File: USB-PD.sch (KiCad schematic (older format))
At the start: 59 parts, among them IC3 TPS7A0518PDBVT, J1 1053131102, J11 E8124-015-01, Q10 Si7223DN, Q11 Si7223DN, Q12 BSS84AKW, Q14 BSS84AKW, Q9 SQS401EN-T1_BE3, U12 STUSB4500QTR, U14 LTC4418IUF#PBF

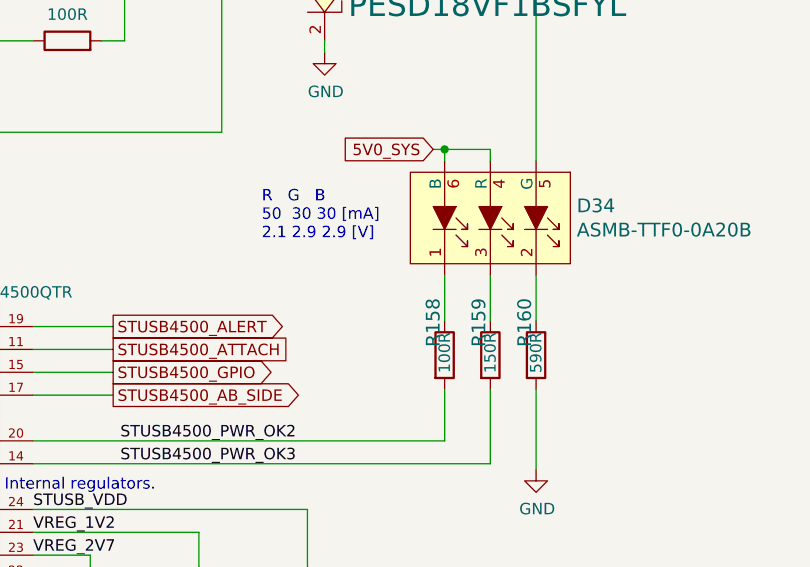
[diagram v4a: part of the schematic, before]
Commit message: Corrected errors from feedback. Added board name, version, Antmicro and OSHW logo, connector labels, button and LED descriptions
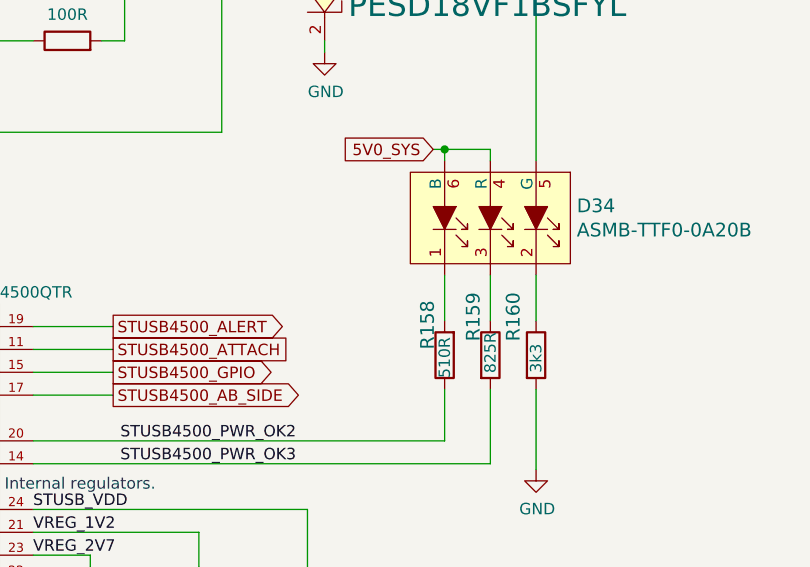
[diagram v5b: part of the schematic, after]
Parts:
- removed R158: R_100R_0402, sc606-baseboard-footprints:0402-res, symbol sc606-baseboard:R_100R_0402
- removed R159: R_150R_0402, sc606-baseboard-footprints:0402-res, symbol sc606-baseboard:R_150R_0402
- removed R160: R_590R_0402, sc606-baseboard-footprints:0402-res, symbol sc606-baseboard:R_590R_0402
- added R158: R_510R_0402, antmicro-footprints:0402-res, symbol antmicroResistors0402:R_510R_0402
- added R159: R_825R_0402, antmicro-footprints:0402-res, symbol antmicroResistors0402:R_825R_0402
- added R160: R_3k3_0402, antmicro-footprints:0402-res, symbol antmicroResistors0402:R_3k3_0402
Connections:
- net GND: now also R160.2
- net STUSB4500_PWR_OK2: now also R158.1
- net STUSB4500_PWR_OK3: now also R159.2
- net at D34.1: now also R158.2
- net at D34.2: now also R160.1
- net at D34.3: now also R159.1
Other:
- note removed: "R G B\n50 30 30 [mA]\n2.1 2.9 2.9 [V]"
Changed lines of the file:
@@
-	0    1    1    0
-$EndComp
-$Comp
-L sc606-baseboard:R_100R_0402 R158
-U 1 1 6219BF48
-P 9900 2975
-F 0 "R158" H 9650 2925 60  0000 L CNN
-F 1 "R_100R_0402" H 9900 2825 60  0001 C CNN
-F 2 "sc606-baseboard-footprints:0402-res" H 10100 3175 60  0001 L CNN
-F 3 "" H 9900 2975 50  0001 C CNN
-F 4 "BOURNS" H 10100 3375 60  0001 L CNN "Manufacturer"
-F 5 "CR0402-FX-1000GLF" H 10100 3275 60  0001 L CNN "MPN"
-F 6 "100R" H 9800 2975 50  0000 L CNN "Val"
-	1    9900 2975
-	0    1    1    0
-$EndComp
-$Comp
-L sc606-baseboard:R_150R_0402 R159
-U 1 1 62198F27
-P 10100 2975
-F 0 "R159" H 9850 2925 60  0000 L CNN
-F 1 "R_150R_0402" H 10100 2825 60  0001 C CNN
-F 2 "sc606-baseboard-footprints:0402-res" H 10300 3175 60  0001 L CNN
-F 3 "" H 10100 2975 50  0001 C CNN
-F 4 "VISHAY" H 10300 3375 60  0001 L CNN "Manufacturer"
-F 5 "CRCW0402150RFKED" H 10300 3275 60  0001 L CNN "MPN"
-F 6 "150R" H 10000 2975 50  0000 L CNN "Val"
-	1    10100 2975
 	0    1    1    0
 $EndComp
@@
 Wire Wire Line
 	10300 2825 10300 2625
-$Comp
-L sc606-baseboard:R_590R_0402 R160
-U 1 1 621057A9
-P 10300 2975
-F 0 "R160" H 10050 2925 60  0000 L CNN
-F 1 "R_590R_0402" H 10300 2825 60  0001 C CNN
-F 2 "sc606-baseboard-footprints:0402-res" H 10500 3175 60  0001 L CNN
-F 3 "" H 10300 2975 50  0001 C CNN
-F 4 "PANASONIC_ELECTRONIC_COMPONENTS" H 10500 3375 60  0001 L CNN "Manufacturer"
-F 5 "ERJ2RKF5900X" H 10500 3275 60  0001 L CNN "MPN"
-F 6 "590R" H 10200 2975 50  0000 L CNN "Val"
-	1    10300 2975
-	0    1    1    0
-$EndComp
 Text GLabel 9850 2075 0    50   Input ~ 0
 5V0_SYS
-Text Notes 9100 2475 0    50   ~ 0
-R   G   B\n50  30 30 [mA]\n2.1 2.9 2.9 [V]
 Wire Wire Line
 	7650 2000 8925 2000
@@
 	1    0    0    1
 $EndComp
+$Comp
+L antmicroResistors0402:R_510R_0402 R158
+U 1 1 622D2DA1
+P 9900 2975
+F 0 "R158" H 9925 3050 60  0000 L CNN
+F 1 "R_510R_0402" H 9900 2825 60  0001 C CNN
+F 2 "antmicro-footprints:0402-res" H 10100 3175 60  0001 L CNN
+F 3 "" H 9900 2975 50  0001 C CNN
+F 4 "Yageo" H 10100 3375 60  0001 L CNN "Manufacturer"
+F 5 "RC0402JR-07510RL" H 10100 3275 60  0001 L CNN "MPN"
+F 6 "510R" H 9800 2975 50  0000 L CNN "Val"
+	1    9900 2975
+	0    -1   -1   0
+$EndComp
+$Comp
+L antmicroResistors0402:R_825R_0402 R159
+U 1 1 622D800C
+P 10100 2975
+F 0 "R159" H 9825 2900 60  0000 L CNN
+F 1 "R_825R_0402" H 10100 2825 60  0001 C CNN
+F 2 "antmicro-footprints:0402-res" H 10300 3175 60  0001 L CNN
+F 3 "" H 10100 2975 50  0001 C CNN
+F 4 "PANASONIC" H 10300 3375 60  0001 L CNN "Manufacturer"
+F 5 "ERJ2RKF8250X" H 10300 3275 60  0001 L CNN "MPN"
+F 6 "825R" H 10000 2975 50  0000 L CNN "Val"
+	1    10100 2975
+	0    1    1    0
+$EndComp
+$Comp
+L antmicroResistors0402:R_3k3_0402 R160
+U 1 1 623007ED
+P 10300 2975
+F 0 "R160" H 10025 2875 60  0000 L CNN
+F 1 "R_3k3_0402" H 10300 2825 60  0001 C CNN
+F 2 "antmicro-footprints:0402-res" H 10500 3175 60  0001 L CNN
+F 3 "" H 10300 2975 50  0001 C CNN
+F 4 "MULTICOMP PRO" H 10500 3375 60  0001 L CNN "Manufacturer"
+F 5 "MCWR04X3301FTL" H 10500 3275 60  0001 L CNN "MPN"
+F 6 "3k3" H 10250 2975 50  0000 L CNN "Val"
+	1    10300 2975
+	0    1    1    0
+$EndComp
 $EndSCHEMATC

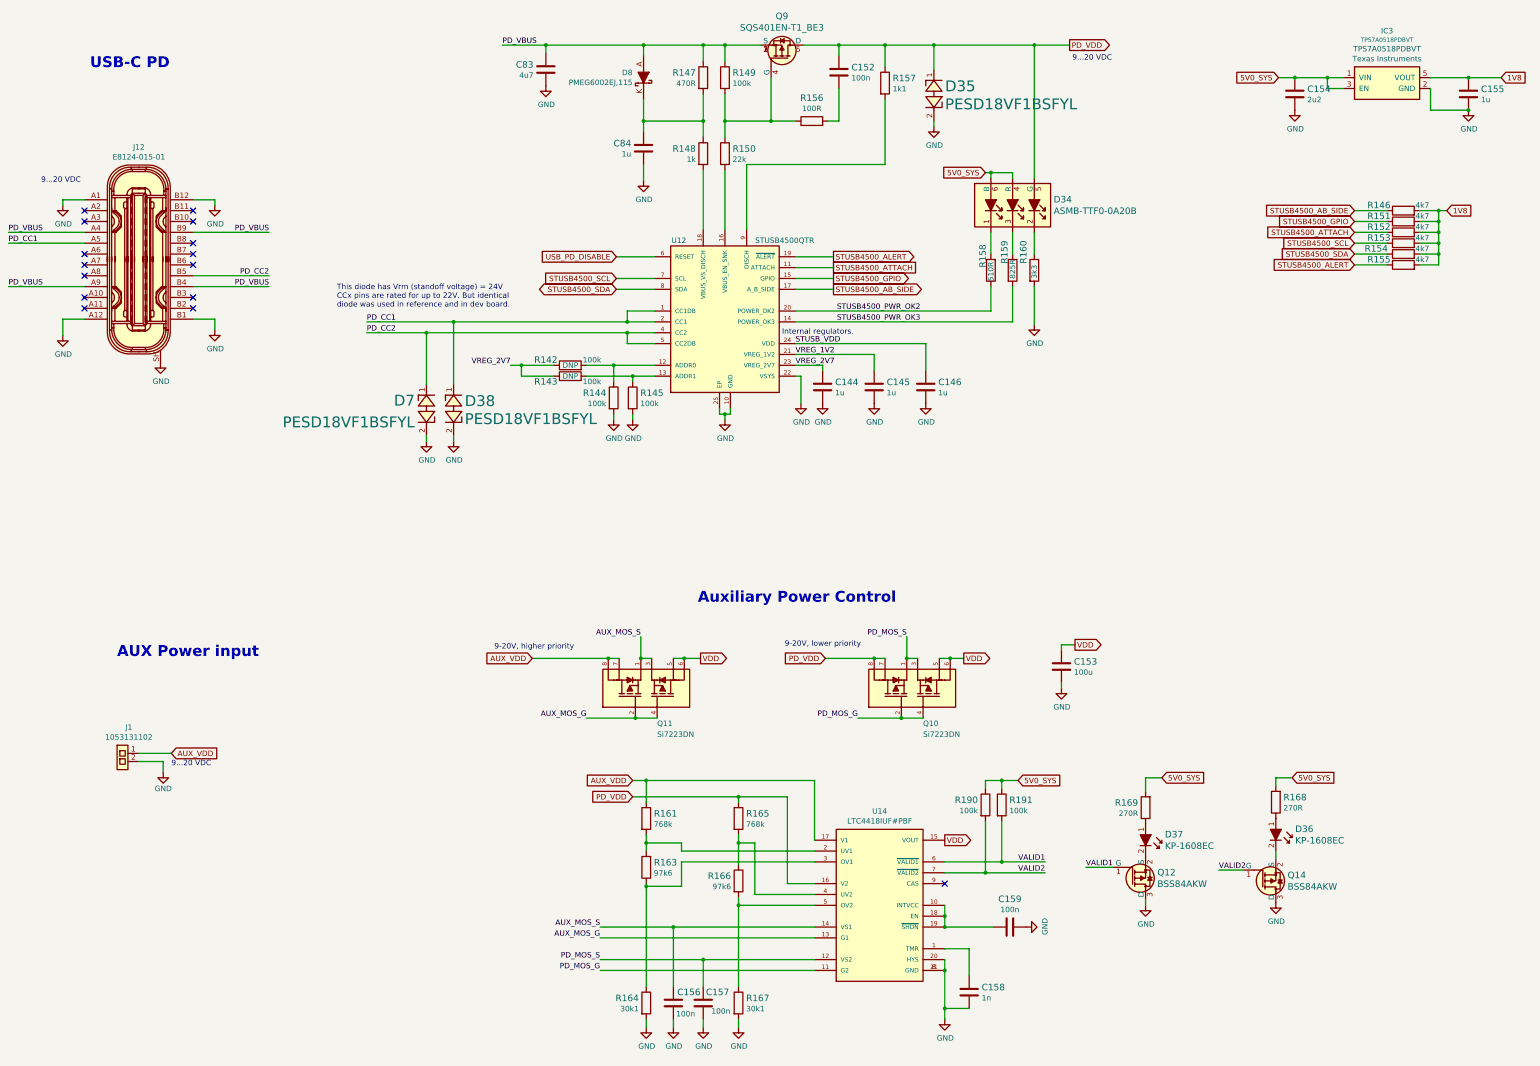
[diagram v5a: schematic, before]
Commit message: Schematic cleanup - peripherals and USB-PD
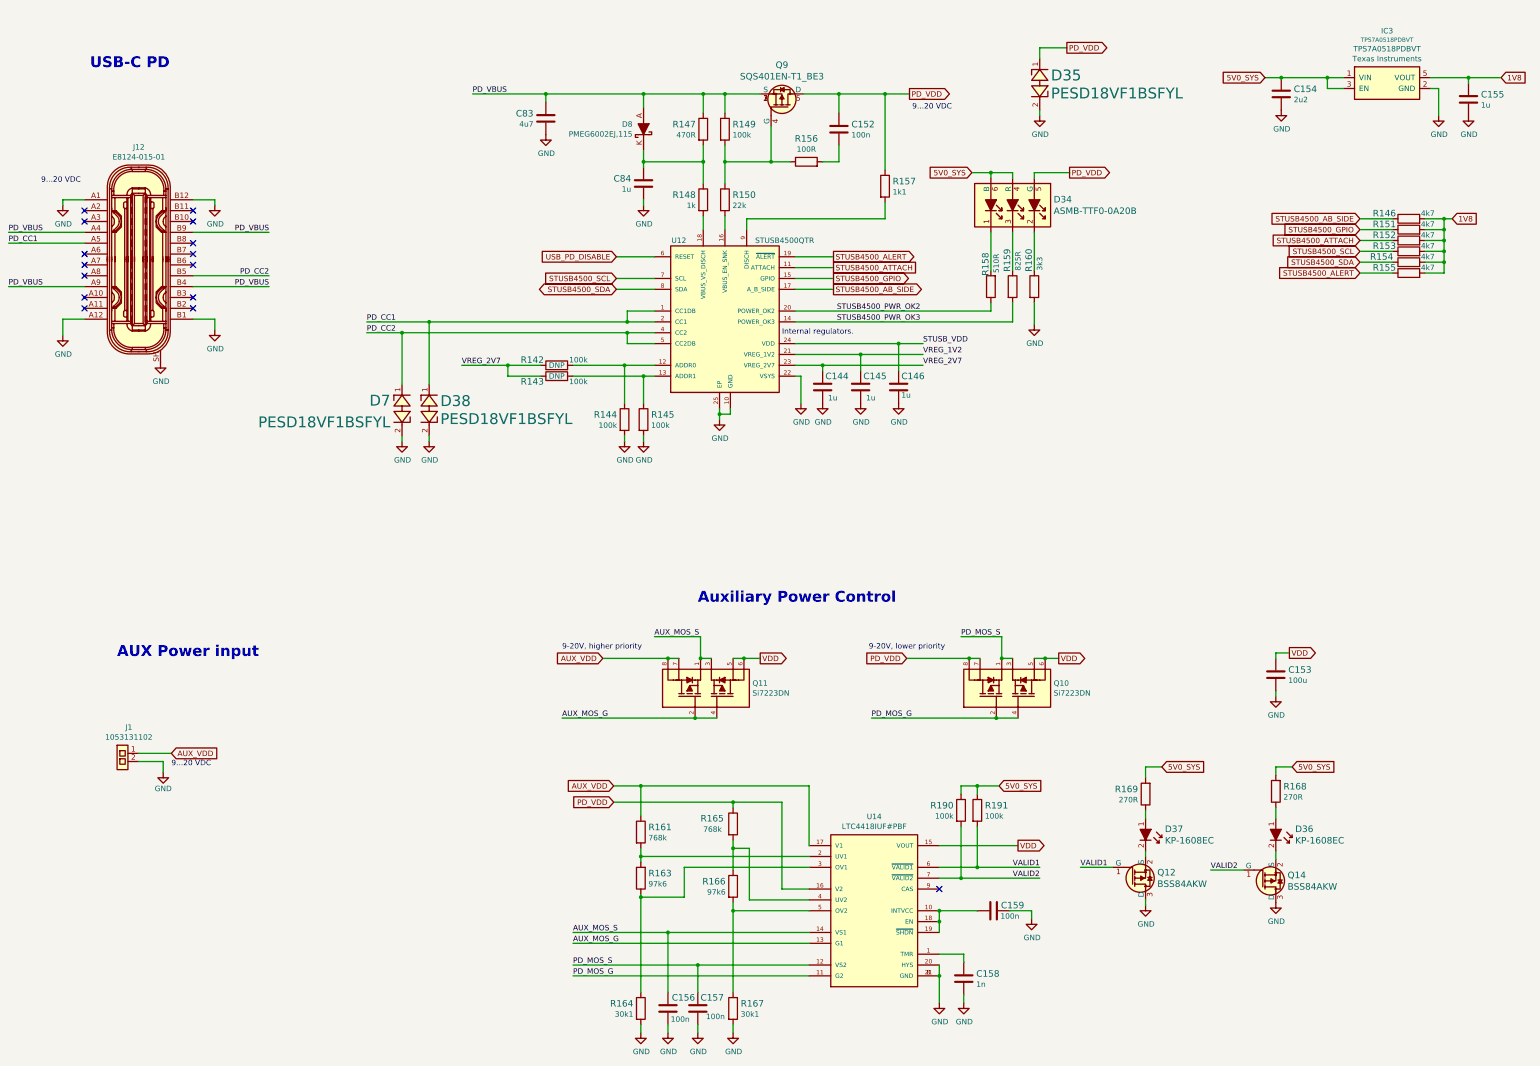
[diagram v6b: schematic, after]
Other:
- note removed: "This diode has Vrm (standoff voltage) = 24V\nCCx pins are rated for up to 22V. But identical\ndiode was used in reference and in dev board."
- moved on the sheet: C145, C146, C152, C153, C154, C155, C156, C157, C158, C159, C83, C84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

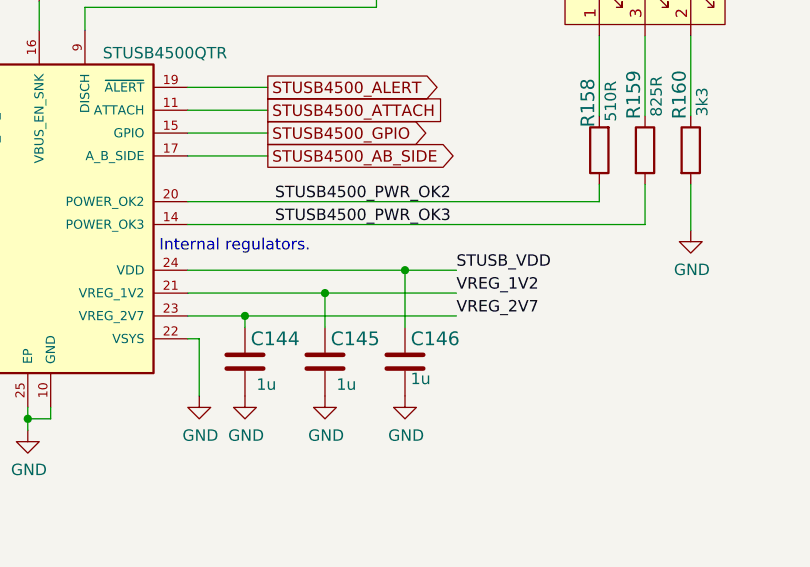
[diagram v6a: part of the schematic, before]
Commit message: Fix STUSB4500 VDD connection, fix DRC error
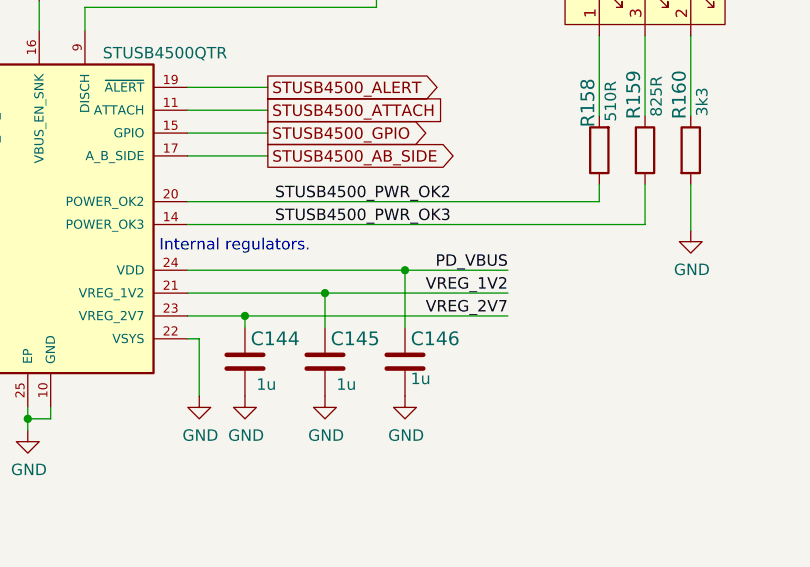
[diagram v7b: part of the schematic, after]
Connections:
- net STUSB_VDD is gone; now on net PD_VBUS: C146.1, U12.24 (VDD)
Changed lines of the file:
@@
 	1    0    0    -1
 $EndComp
-Text Label 9275 3850 0    50   ~ 0
+Text Label 9500 3850 2    50   ~ 0
 VREG_2V7
-Text Label 9275 3750 0    50   ~ 0
+Text Label 9500 3750 2    50   ~ 0
 VREG_1V2
-Text Label 9275 3650 0    50   ~ 0
-STUSB_VDD
 Connection ~ 6700 1350
 Wire Wire Line
@@
 	7400 4300 7500 4300
 Wire Wire Line
-	9275 3850 8350 3850
+	9500 3850 8350 3850
 Connection ~ 8350 3850
 Wire Wire Line
-	8700 3750 9275 3750
+	8700 3750 9500 3750
 Connection ~ 8700 3750
 Wire Wire Line
@@
 Connection ~ 9050 3650
 Wire Wire Line
-	9050 3650 9275 3650
+	9050 3650 9500 3650
 Wire Wire Line
 	9150 1350 8925 1350
@@
 Wire Wire Line
 	14025 1300 13950 1300
+Text Label 9500 3650 2    50   ~ 0
+PD_VBUS
 $EndSCHEMATC

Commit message: Corrected footprint of Q10 and Q11. Used 'kmake loclib'
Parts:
- Q12, Q14: footprint antmicro-footprints:SOT-323 -> sc606-baseboard-footprints:SOT-323; symbol antmicroTransistorsFETsMOSFETsSingle:BSS84AKW -> sc606-baseboard:BSS84AKW
- R158: footprint antmicro-footprints:0402-res -> sc606-baseboard-footprints:0402-res; symbol antmicroResistors0402:R_510R_0402 -> sc606-baseboard:R_510R_0402
- R159: footprint antmicro-footprints:0402-res -> sc606-baseboard-footprints:0402-res; symbol antmicroResistors0402:R_825R_0402 -> sc606-baseboard:R_825R_0402
- R160: footprint antmicro-footprints:0402-res -> sc606-baseboard-footprints:0402-res; symbol antmicroResistors0402:R_3k3_0402 -> sc606-baseboard:R_3k3_0402
- R190, R191: footprint antmicro-footprints:0402-res -> sc606-baseboard-footprints:0402-res; symbol antmicroResistors0402:R_100k_0402 -> sc606-baseboard:R_100k_0402
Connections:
- net AUX_VDD: now also Q11.5, Q11.6; no longer Q11.7, Q11.8
- net PD_VDD: now also Q10.5, Q10.6; no longer Q10.7, Q10.8
- net VDD: now also Q10.7, Q10.8, Q11.7, Q11.8; no longer Q10.5, Q10.6, Q11.5, Q11.6
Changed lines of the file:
@@
 F 5 "VISHAY" H 6675 6850 50  0001 C CNN "Manufacturer"
 	1    7275 6800
-	0    -1   -1   0
+	0    1    -1   0
 $EndComp
 $Comp
@@
 F 5 "VISHAY" H 9450 6850 50  0001 C CNN "Manufacturer"
 	1    10050 6800
-	0    -1   -1   0
+	0    1    -1   0
 $EndComp
 Wire Wire Line
@@
 	9425 8875 9775 8875
 $Comp
-L antmicroResistors0402:R_100k_0402 R191
+L sc606-baseboard:R_100k_0402 R191
 U 1 1 62642D75
 P 9775 7950
 F 0 "R191" V 9730 8020 60  0000 L CNN
 F 1 "R_100k_0402" H 9775 7800 60  0001 C CNN
-F 2 "antmicro-footprints:0402-res" H 9975 8150 60  0001 L CNN
+F 2 "sc606-baseboard-footprints:0402-res" H 9975 8150 60  0001 L CNN
 F 3 "" H 9775 7950 50  0001 C CNN
 F 4 "VISHAY" H 9975 8350 60  0001 L CNN "Manufacturer"
@@
 	9775 7725 9775 7800
 $Comp
-L antmicroResistors0402:R_100k_0402 R190
+L sc606-baseboard:R_100k_0402 R190
 U 1 1 6266023E
 P 9625 7950
 F 0 "R190" V 9580 7881 60  0000 R CNN
 F 1 "R_100k_0402" H 9625 7800 60  0001 C CNN
-F 2 "antmicro-footprints:0402-res" H 9825 8150 60  0001 L CNN
+F 2 "sc606-baseboard-footprints:0402-res" H 9825 8150 60  0001 L CNN
 F 3 "" H 9625 7950 50  0001 C CNN
 F 4 "VISHAY" H 9825 8350 60  0001 L CNN "Manufacturer"
@@
 5V0_SYS
 $Comp
-L antmicroTransistorsFETsMOSFETsSingle:BSS84AKW Q14
+L sc606-baseboard:BSS84AKW Q14
 U 1 1 6293D495
 P 12525 8600
 F 0 "Q14" H 12633 8547 60  0000 L CNN
 F 1 "BSS84AKW" H 12633 8653 60  0000 L CNN
-F 2 "antmicro-footprints:SOT-323" H 12725 8800 60  0001 L CNN
+F 2 "sc606-baseboard-footprints:SOT-323" H 12725 8800 60  0001 L CNN
 F 3 "https://pl.mouser.com/datasheet/2/916/BSS84AKW-1320023.pdf" H 12725 8900 60  0001 L CNN
 F 4 "BSS84AKW,115" H 12725 9100 60  0001 L CNN "MPN"
@@
 $EndComp
 $Comp
-L antmicroTransistorsFETsMOSFETsSingle:BSS84AKW Q12
+L sc606-baseboard:BSS84AKW Q12
 U 1 1 6293FDAB
 P 11325 8575
 F 0 "Q12" H 11433 8522 60  0000 L CNN
 F 1 "BSS84AKW" H 11433 8628 60  0000 L CNN
-F 2 "antmicro-footprints:SOT-323" H 11525 8775 60  0001 L CNN
+F 2 "sc606-baseboard-footprints:SOT-323" H 11525 8775 60  0001 L CNN
 F 3 "https://pl.mouser.com/datasheet/2/916/BSS84AKW-1320023.pdf" H 11525 8875 60  0001 L CNN
 F 4 "BSS84AKW,115" H 11525 9075 60  0001 L CNN "MPN"
@@
 $EndComp
 $Comp
-L antmicroResistors0402:R_510R_0402 R158
+L sc606-baseboard:R_510R_0402 R158
 U 1 1 622D2DA1
 P 9900 3125
 F 0 "R158" H 10000 3175 60  0000 L CNN
 F 1 "R_510R_0402" H 9900 2975 60  0001 C CNN
-F 2 "antmicro-footprints:0402-res" H 10100 3325 60  0001 L CNN
+F 2 "sc606-baseboard-footprints:0402-res" H 10100 3325 60  0001 L CNN
 F 3 "" H 9900 3125 50  0001 C CNN
 F 4 "Yageo" H 10100 3525 60  0001 L CNN "Manufacturer"
@@
 $EndComp
 $Comp
-L antmicroResistors0402:R_825R_0402 R159
+L sc606-baseboard:R_825R_0402 R159
 U 1 1 622D800C
 P 10100 3125
 F 0 "R159" H 9750 3075 60  0000 L CNN
 F 1 "R_825R_0402" H 10100 2975 60  0001 C CNN
-F 2 "antmicro-footprints:0402-res" H 10300 3325 60  0001 L CNN
+F 2 "sc606-baseboard-footprints:0402-res" H 10300 3325 60  0001 L CNN
 F 3 "" H 10100 3125 50  0001 C CNN
 F 4 "PANASONIC" H 10300 3525 60  0001 L CNN "Manufacturer"
@@
 $EndComp
 $Comp
-L antmicroResistors0402:R_3k3_0402 R160
+L sc606-baseboard:R_3k3_0402 R160
 U 1 1 623007ED
 P 10300 3125
 F 0 "R160" H 9950 3075 60  0000 L CNN
 F 1 "R_3k3_0402" H 10300 2975 60  0001 C CNN
-F 2 "antmicro-footprints:0402-res" H 10500 3325 60  0001 L CNN
+F 2 "sc606-baseboard-footprints:0402-res" H 10500 3325 60  0001 L CNN
 F 3 "" H 10300 3125 50  0001 C CNN
 F 4 "MULTICOMP PRO" H 10500 3525 60  0001 L CNN "Manufacturer"
@@
 AR Path="/62A770DC" Ref="#PWR?"  Part="1"
 AR Path="/61B0DC30/62A770DC" Ref="#PWR?"  Part="1"
-AR Path="/623AED4D/62A770DC" Ref="#PWR?"  Part="1"
-F 0 "#PWR?" H 9650 9475 50  0001 C CNN
+AR Path="/623AED4D/62A770DC" Ref="#PWR0255"  Part="1"
+F 0 "#PWR0255" H 9650 9475 50  0001 C CNN
 F 1 "GND" H 9655 9552 50  0000 C CNN
 F 2 "" H 9650 9725 50  0001 C CNN
@@
 P 14025 1550
 AR Path="/61F60810/62F95540" Ref="#PWR?"  Part="1"
-AR Path="/623AED4D/62F95540" Ref="#PWR?"  Part="1"
-F 0 "#PWR?" H 14025 1300 50  0001 C CNN
+AR Path="/623AED4D/62F95540" Ref="#PWR0256"  Part="1"
+F 0 "#PWR0256" H 14025 1300 50  0001 C CNN
 F 1 "GND" H 14030 1377 50  0000 C CNN
 F 2 "" H 14025 1550 50  0001 C CNN
